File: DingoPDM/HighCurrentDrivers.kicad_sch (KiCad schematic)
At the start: 0 parts

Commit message: V5 As Built
-Changed ADS1015 to MAX11613EUA+T due to supply issues
-Changed PCB to match JLCPCB 2oz rules
-Changed ON_SW input to 12V switched
-Switched to TagConnect TC2030
-Changed pin positions of GND, IN1, IN2
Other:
- title: (none) -> Dingo_PDM
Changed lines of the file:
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@@
 (kicad_sch (version 20230121) (generator eeschema)
   (paper "A4")
+  (title_block
+    (title "Dingo_PDM")
+    (date "2023-02-23")
+    (rev "v5")
+    (comment 3 "github.com/corygrant")
+    (comment 4 "Cory Grant")
+  )
   (wire (pts (xy 63.5 124.46) (xy 66.04 124.46))
     (stroke (width 0) (type default))
@@
     (instances
       (project "DingoPDM"
-        (path "/8948e307-9174-4227-9c28-3ff885e6e83d/00000000-0000-0000-0000-00005f54b02a" (page "10"))
+        (path "/8948e307-9174-4227-9c28-3ff885e6e83d/00000000-0000-0000-0000-00005f54b02a" (page "8"))
       )
     )
@@
     (instances
       (project "DingoPDM"
-        (path "/8948e307-9174-4227-9c28-3ff885e6e83d/00000000-0000-0000-0000-00005f54b02a" (page "11"))
+        (path "/8948e307-9174-4227-9c28-3ff885e6e83d/00000000-0000-0000-0000-00005f54b02a" (page "9"))
       )
     )
@@
     (instances
       (project "DingoPDM"
-        (path "/8948e307-9174-4227-9c28-3ff885e6e83d/00000000-0000-0000-0000-00005f54b02a" (page "12"))
+        (path "/8948e307-9174-4227-9c28-3ff885e6e83d/00000000-0000-0000-0000-00005f54b02a" (page "10"))
       )
     )
@@
     (instances
       (project "DingoPDM"
-        (path "/8948e307-9174-4227-9c28-3ff885e6e83d/00000000-0000-0000-0000-00005f54b02a" (page "13"))
-      )
-    )
+        (path "/8948e307-9174-4227-9c28-3ff885e6e83d/00000000-0000-0000-0000-00005f54b02a" (page "11"))
+      )
+    )

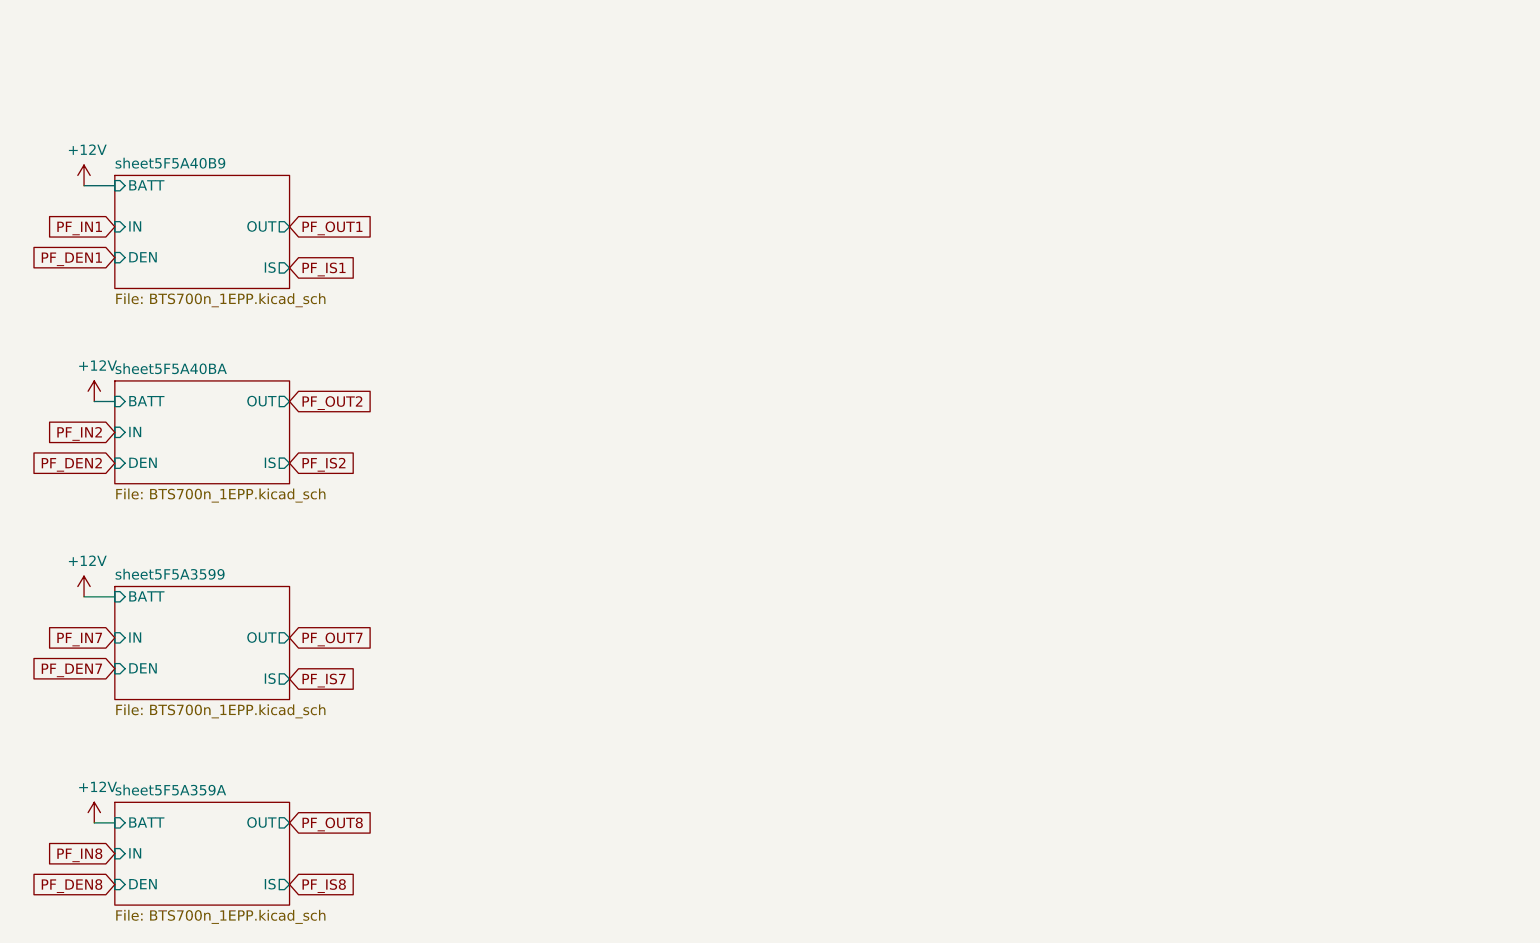
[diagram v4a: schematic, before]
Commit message: Redesigned to a smaller unit
4x high current, 2x med current, 4x low current, 2x digital inputs
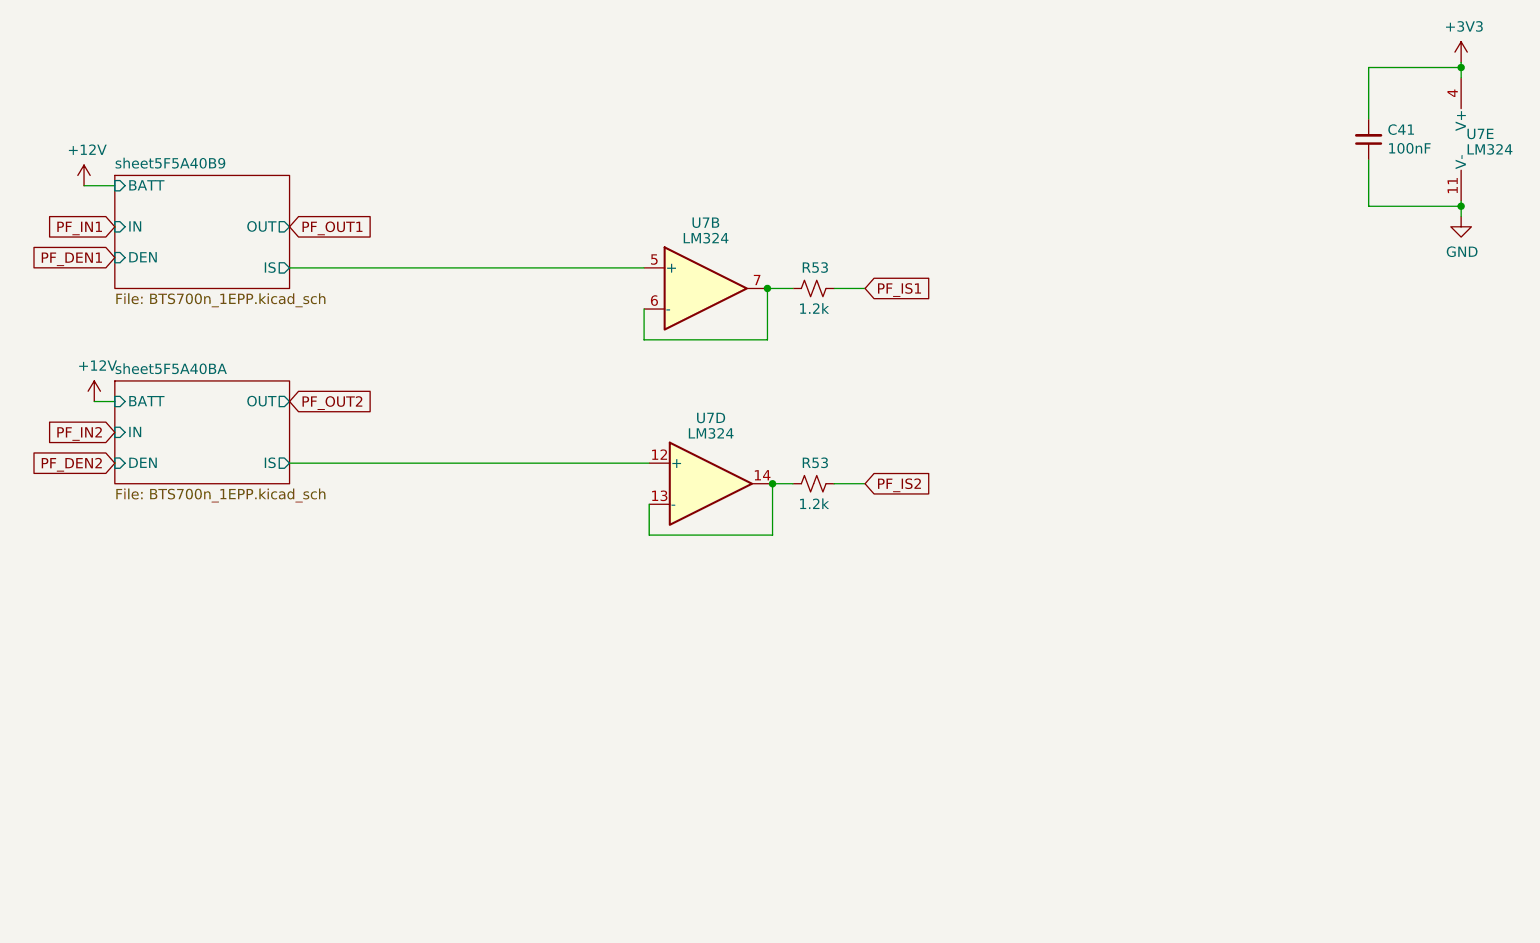
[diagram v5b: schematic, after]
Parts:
- added C41: 100nF, Capacitor_SMD:C_0805_2012Metric, symbol Device:C_Small
- added R53 (x2): 1.2k, Resistor_SMD:R_0805_2012Metric, symbol Device:R_Small_US
- added U7: LM324, Package_SO:TSSOP-14_4.4x5mm_P0.65mm, symbol Amplifier_Operational:LM324
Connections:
- net PF_IS1: now also R53.2
- net PF_IS2: now also R53.2
- new net: R53.1, U7.13 (-), U7.14
- new net: R53.1, U7.6 (-), U7.7
- new net +3V3: C41.2, U7.4 (V+)
- new net GND: C41.1, U7.11 (V-)
- new net sheet5F5A40B9/IS: U7.5 (+)
- new net sheet5F5A40BA/IS: U7.12 (+)
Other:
- removed sheet sheet5F5A3599
- removed sheet sheet5F5A359A

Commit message: Added documentation, finished and cleaned design
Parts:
- R53: LCSC (none) -> C727987
- U7: Digi-Key_PN (none) -> 497-7330-1-ND; LCSC (none) -> C7944
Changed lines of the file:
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@@
   (title_block
     (title "Dingo_PDM")
-    (date "2023-04-01")
-    (rev "v5")
+    (date "2023-07-28")
+    (rev "v6")
     (comment 3 "github.com/corygrant")
     (comment 4 "Cory Grant")
@@
       (effects (font (size 1.27 1.27)) hide)
     )
-    (property "LCSC" "" (at 152.4 82.55 0)
+    (property "LCSC" "C727987" (at 152.4 82.55 0)
       (effects (font (size 1.27 1.27)) hide)
     )
@@
       (effects (font (size 1.27 1.27)) hide)
     )
-    (property "LCSC" "" (at 152.4 58.42 0)
+    (property "LCSC" "C727987" (at 152.4 58.42 0)
       (effects (font (size 1.27 1.27)) hide)
     )
@@
     )
     (property "Datasheet" "http://www.ti.com/lit/ds/symlink/lm2902-n.pdf" (at 140.335 53.34 0)
+      (effects (font (size 1.27 1.27)) hide)
+    )
+    (property "Digi-Key_PN" "497-7330-1-ND" (at 139.065 58.42 0)
+      (effects (font (size 1.27 1.27)) hide)
+    )
+    (property "LCSC" "C7944" (at 139.065 58.42 0)
       (effects (font (size 1.27 1.27)) hide)
     )
@@
       (effects (font (size 1.27 1.27)) hide)
     )
+    (property "Digi-Key_PN" "497-7330-1-ND" (at 139.7 82.55 0)
+      (effects (font (size 1.27 1.27)) hide)
+    )
+    (property "LCSC" "C7944" (at 139.7 82.55 0)
+      (effects (font (size 1.27 1.27)) hide)
+    )
     (pin "1")
     (pin "2")
@@
       (effects (font (size 1.27 1.27)) hide)
     )
+    (property "Digi-Key_PN" "497-7330-1-ND" (at 234.95 40.005 0)
+      (effects (font (size 1.27 1.27)) hide)
+    )
+    (property "LCSC" "C7944" (at 234.95 40.005 0)
+      (effects (font (size 1.27 1.27)) hide)
+    )

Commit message: Routed V7
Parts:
- removed R53 (x2): 1.2k, Resistor_SMD:R_0805_2012Metric, symbol Device:R_Small_US
- added R8 (x2): 120R, Resistor_SMD:R_0805_2012Metric, symbol Device:R_Small_US
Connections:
- net PF_IS1: now also R8.1
- net PF_IS2: now also R8.1
- net at U7.13 (-), U7.14: now also R8.2
- net at U7.6 (-), U7.7: now also R8.2
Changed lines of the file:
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@@
     )
   )
-  (symbol (lib_id "Device:R_Small_US") (at 152.4 82.55 90) (unit 1)
+  (symbol (lib_id "Device:R_Small_US") (at 152.4 58.42 270) (unit 1)
     (in_bom yes) (on_board yes) (dnp no)
-    (property "Reference" "R53" (at 154.305 80.01 90)
-      (effects (font (size 1.27 1.27)) (justify left))
+    (property "Reference" "R8" (at 152.4 53.213 90)
+      (effects (font (size 1.27 1.27)))
     )
-    (property "Value" "1.2k" (at 154.305 85.09 90)
-      (effects (font (size 1.27 1.27)) (justify left))
+    (property "Value" "120R" (at 152.4 55.5244 90)
+      (effects (font (size 1.27 1.27)))
+    )
+    (property "Footprint" "Resistor_SMD:R_0805_2012Metric" (at 152.4 58.42 0)
+      (effects (font (size 1.27 1.27)) hide)
+    )
+    (property "Datasheet" "" (at 152.4 58.42 0)
+      (effects (font (size 1.27 1.27)) hide)
+    )
+    (property "Digi-Key_PN" "311-120CRCT-ND" (at 152.4 58.42 0)
+      (effects (font (size 1.27 1.27)) hide)
+    )
+    (property "LCSC" "C229076" (at 152.4 58.42 0)
+      (effects (font (size 1.27 1.27)) hide)
+    )
+    (pin "1")
+    (pin "2")
+    (instances
+      (project "DingoPDM"
+        (path "/8948e307-9174-4227-9c28-3ff885e6e83d/00000000-0000-0000-0000-00005f5b7065"
+          (reference "R8") (unit 1)
+        )
+        (path "/8948e307-9174-4227-9c28-3ff885e6e83d/00000000-0000-0000-0000-00005f54b02a"
+          (reference "R11") (unit 1)
+        )
+      )
+    )
+  )
+  (symbol (lib_id "Device:R_Small_US") (at 152.4 82.55 270) (unit 1)
+    (in_bom yes) (on_board yes) (dnp no)
+    (property "Reference" "R8" (at 152.4 77.343 90)
+      (effects (font (size 1.27 1.27)))
+    )
+    (property "Value" "120R" (at 152.4 79.6544 90)
+      (effects (font (size 1.27 1.27)))
     )
     (property "Footprint" "Resistor_SMD:R_0805_2012Metric" (at 152.4 82.55 0)
@@
       (effects (font (size 1.27 1.27)) hide)
     )
-    (property "Digi-Key_PN" "311-1.20KCRCT-ND" (at 152.4 82.55 0)
+    (property "Digi-Key_PN" "311-120CRCT-ND" (at 152.4 82.55 0)
       (effects (font (size 1.27 1.27)) hide)
     )
-    (property "LCSC" "C727987" (at 152.4 82.55 0)
+    (property "LCSC" "C229076" (at 152.4 82.55 0)
       (effects (font (size 1.27 1.27)) hide)
     )
@@
     (instances
       (project "DingoPDM"
-        (path "/8948e307-9174-4227-9c28-3ff885e6e83d/00000000-0000-0000-0000-00005f54bf48/00000000-0000-0000-0000-00005f5a9675"
-          (reference "R53") (unit 1)
+        (path "/8948e307-9174-4227-9c28-3ff885e6e83d/00000000-0000-0000-0000-00005f5b7065"
+          (reference "R8") (unit 1)
         )
         (path "/8948e307-9174-4227-9c28-3ff885e6e83d/00000000-0000-0000-0000-00005f54b02a"
@@
         )
       )
-    )
-  )
-  (symbol (lib_id "Device:R_Small_US") (at 152.4 58.42 90) (unit 1)
-    (in_bom yes) (on_board yes) (dnp no)
-    (property "Reference" "R53" (at 154.305 55.88 90)
-      (effects (font (size 1.27 1.27)) (justify left))
-    )
-    (property "Value" "1.2k" (at 154.305 60.96 90)
-      (effects (font (size 1.27 1.27)) (justify left))
-    )
-    (property "Footprint" "Resistor_SMD:R_0805_2012Metric" (at 152.4 58.42 0)
-      (effects (font (size 1.27 1.27)) hide)
-    )
-    (property "Datasheet" "" (at 152.4 58.42 0)
-      (effects (font (size 1.27 1.27)) hide)
-    )
-    (property "Digi-Key_PN" "311-1.20KCRCT-ND" (at 152.4 58.42 0)
-      (effects (font (size 1.27 1.27)) hide)
-    )
-    (property "LCSC" "C727987" (at 152.4 58.42 0)
-      (effects (font (size 1.27 1.27)) hide)
-    )
-    (pin "1")
-    (pin "2")
-    (instances
-      (project "DingoPDM"
-        (path "/8948e307-9174-4227-9c28-3ff885e6e83d/00000000-0000-0000-0000-00005f54bf48/00000000-0000-0000-0000-00005f5a9675"
-          (reference "R53") (unit 1)
-        )
-        (path "/8948e307-9174-4227-9c28-3ff885e6e83d/00000000-0000-0000-0000-00005f54b02a"
-          (reference "R11") (unit 1)
-        )
-      )
